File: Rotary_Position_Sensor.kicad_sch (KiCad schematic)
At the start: 8 parts

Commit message: Ещё доработать
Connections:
- net OUT_MCU: now reaches C4.2, D1.3 (OUT), R2.2
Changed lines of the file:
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@@
   (junction (at 45.72 48.26) (diameter 0) (color 0 0 0 0)
+  )
+  (junction (at 52.07 48.26) (diameter 0) (color 0 0 0 0)
   )
   (no_connect (at 55.88 38.1))
@@
     (stroke (width 0) (type default))
   )
+  (wire (pts (xy 52.07 52.07) (xy 52.07 48.26))
+    (stroke (width 0) (type default))
+  )
   (wire (pts (xy 27.94 40.64) (xy 33.02 40.64))
+    (stroke (width 0) (type default))
+  )
+  (wire (pts (xy 76.2 52.07) (xy 52.07 52.07))
     (stroke (width 0) (type default))
   )
@@
       (effects (font (size 1.27 1.27)) (justify left) hide)
     )
+  )
+  (global_label "OUT_MCU" (shape output) (at 76.2 52.07 0) (fields_autoplaced)
+    (effects (font (size 1.27 1.27)) (justify left))
+    (property "Intersheetrefs" "${INTERSHEET_REFS}" (at 87.7539 52.07 0)
+      (effects (font (size 1.27 1.27)) (justify left) hide)
+    )

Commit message: Собираю документацию
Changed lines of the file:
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@@
   (symbol (lib_id "Hall_Sensor_My:NSM3012") (at 63.5 33.02 0) (unit 1)
     (in_bom yes) (on_board yes) (dnp no) (fields_autoplaced)
-    (property "Reference" "D1" (at 63.5 29.21 0)
+    (property "Reference" "D1" (at 63.5 27.94 0)
       (effects (font (size 1.27 1.27)))
     )
-    (property "Value" "NSM3012" (at 63.5 31.75 0)
+    (property "Value" "NSM3012" (at 63.5 30.48 0)
       (effects (font (size 1.27 1.27)))
     )

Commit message: ...
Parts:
- R1: value 10 -> 0
- R2: value 50 -> 51

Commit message: Версия под отчёт
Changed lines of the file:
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@@
   )
   (symbol (lib_id "Device:C_Small") (at 174.625 99.06 0) (unit 1)
-    (in_bom yes) (on_board yes) (dnp no) (fields_autoplaced)
-    (property "Reference" "C5" (at 177.165 98.4313 0)
-      (effects (font (size 1.27 1.27)) (justify left))
-    )
-    (property "Value" "100n" (at 177.165 100.9713 0)
+    (in_bom yes) (on_board yes) (dnp no)
+    (property "Reference" "C5" (at 176.53 97.79 0)
+      (effects (font (size 1.27 1.27)) (justify left))
+    )
+    (property "Value" "100n" (at 176.53 100.33 0)
       (effects (font (size 1.27 1.27)) (justify left))
     )
@@
         )
         (path "/69677e3f-3942-4c93-9a5c-92669e2df5eb/bcde038a-9c61-4256-93bc-e646290f2e91"
-          (reference "C1") (unit 1)
+          (reference "C5") (unit 1)
         )
         (path "/69677e3f-3942-4c93-9a5c-92669e2df5eb/555e8538-1d60-4a85-8162-4c8254aec889"
@@
   (symbol (lib_id "Device:R_Small") (at 137.795 96.52 90) (unit 1)
     (in_bom yes) (on_board yes) (dnp no)
-    (property "Reference" "R1" (at 137.795 93.98 90)
-      (effects (font (size 1.27 1.27)))
-    )
-    (property "Value" "0" (at 137.795 99.06 90)
+    (property "Reference" "R1" (at 137.795 94.615 90)
+      (effects (font (size 1.27 1.27)))
+    )
+    (property "Value" "0" (at 137.795 98.425 90)
       (effects (font (size 1.27 1.27)))
     )
@@
   (symbol (lib_id "Device:C_Small") (at 131.445 107.95 0) (unit 1)
     (in_bom yes) (on_board yes) (dnp no)
-    (property "Reference" "C2" (at 126.365 106.68 0)
+    (property "Reference" "C2" (at 127.635 106.68 0)
       (effects (font (size 1.27 1.27)) (justify left))
     )
@@
         )
         (path "/69677e3f-3942-4c93-9a5c-92669e2df5eb/bcde038a-9c61-4256-93bc-e646290f2e91"
-          (reference "C4") (unit 1)
+          (reference "C2") (unit 1)
         )
         (path "/69677e3f-3942-4c93-9a5c-92669e2df5eb/555e8538-1d60-4a85-8162-4c8254aec889"
@@
   (symbol (lib_id "Device:C_Small") (at 144.145 107.95 0) (unit 1)
     (in_bom yes) (on_board yes) (dnp no)
-    (property "Reference" "C4" (at 145.415 106.68 0)
-      (effects (font (size 1.27 1.27)) (justify left))
-    )
-    (property "Value" "100n" (at 145.415 109.22 0)
+    (property "Reference" "C4" (at 146.05 106.68 0)
+      (effects (font (size 1.27 1.27)) (justify left))
+    )
+    (property "Value" "100n" (at 146.05 109.22 0)
       (effects (font (size 1.27 1.27)) (justify left))
     )
@@
         )
         (path "/69677e3f-3942-4c93-9a5c-92669e2df5eb/bcde038a-9c61-4256-93bc-e646290f2e91"
-          (reference "C5") (unit 1)
+          (reference "C4") (unit 1)
         )
         (path "/69677e3f-3942-4c93-9a5c-92669e2df5eb/555e8538-1d60-4a85-8162-4c8254aec889"
@@
   (symbol (lib_id "Device:C_Small") (at 131.445 100.33 0) (unit 1)
     (in_bom yes) (on_board yes) (dnp no)
-    (property "Reference" "C1" (at 126.365 99.06 0)
+    (property "Reference" "C1" (at 127.635 99.06 0)
       (effects (font (size 1.27 1.27)) (justify left))
     )
@@
         )
         (path "/69677e3f-3942-4c93-9a5c-92669e2df5eb/bcde038a-9c61-4256-93bc-e646290f2e91"
-          (reference "C2") (unit 1)
+          (reference "C1") (unit 1)
         )
         (path "/69677e3f-3942-4c93-9a5c-92669e2df5eb/555e8538-1d60-4a85-8162-4c8254aec889"
@@
   (symbol (lib_id "Device:C_Small") (at 144.145 100.33 0) (unit 1)
     (in_bom yes) (on_board yes) (dnp no)
-    (property "Reference" "C3" (at 145.415 99.06 0)
-      (effects (font (size 1.27 1.27)) (justify left))
-    )
-    (property "Value" "100n" (at 145.415 101.6 0)
+    (property "Reference" "C3" (at 146.05 99.06 0)
+      (effects (font (size 1.27 1.27)) (justify left))
+    )
+    (property "Value" "100n" (at 146.05 101.6 0)
       (effects (font (size 1.27 1.27)) (justify left))
     )
@@
   (symbol (lib_id "Device:R_Small") (at 137.795 111.76 90) (unit 1)
     (in_bom yes) (on_board yes) (dnp no)
-    (property "Reference" "R2" (at 137.795 109.22 90)
-      (effects (font (size 1.27 1.27)))
-    )
-    (property "Value" "51" (at 137.795 114.3 90)
-      (effects (font (size 1.27 1.27)))
-    )
+    (property "Reference" "R2" (at 137.795 109.855 90)
+      (effects (font (size 1.27 1.27)))
+    )
+    (property "Value" "51" (at 137.795 113.665 90)
+      (effects (font (size 1.27 1.27)))
+    )

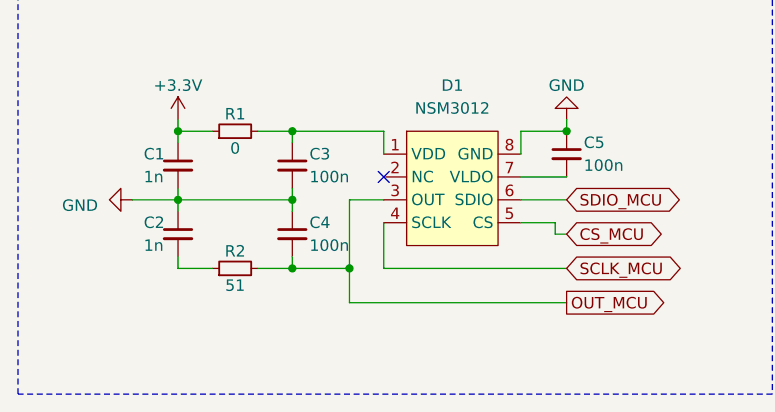
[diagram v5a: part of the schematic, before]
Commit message: Изменил разводку шунтов, вывел выход датчика положения после фильтра
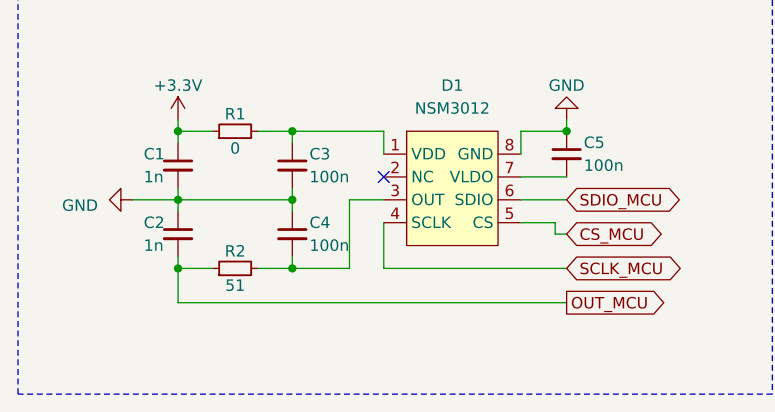
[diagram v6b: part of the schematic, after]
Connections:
- net OUT_MCU: now also C2.2, R2.1; no longer C4.2, D1.3 (OUT), R2.2
- new net: C4.2, D1.3 (OUT), R2.2
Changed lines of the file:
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@@
   (paper "A4")
   (title_block
-    (comment 1 "МПСТ.76721.758764.03.Э3.М")
+    (comment 1 "МПСТ.76721.758764.03.М Э3")
   )
   (junction (at 144.145 111.76) (diameter 0) (color 0 0 0 0)
@@
   (junction (at 131.445 104.14) (diameter 0) (color 0 0 0 0)
   )
-  (junction (at 150.495 111.76) (diameter 0) (color 0 0 0 0)
+  (junction (at 131.445 111.76) (diameter 0) (color 0 0 0 0)
   )
   (no_connect (at 154.305 101.6))
@@
     (stroke (width 0) (type default))
   )
-  (wire (pts (xy 174.625 115.57) (xy 150.495 115.57))
+  (wire (pts (xy 131.445 115.57) (xy 174.625 115.57))
     (stroke (width 0) (type default))
   )
@@
     (stroke (width 0) (type default))
   )
-  (wire (pts (xy 150.495 115.57) (xy 150.495 111.76))
-    (stroke (width 0) (type default))
-  )
   (wire (pts (xy 169.545 104.14) (xy 174.625 104.14))
     (stroke (width 0) (type default))
@@
     (stroke (width 0) (type default))
   )
+  (wire (pts (xy 131.445 115.57) (xy 131.445 111.76))
+    (stroke (width 0) (type default))
+  )

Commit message: VER2.0
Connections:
- net +3.3V renamed +3.3VA
- net CS_MCU: no longer names the net of D1.5 (CS)
- net GND renamed GNDA
- net SCLK_MCU: no longer names the net of D1.4 (SCLK)
- net SDIO_MCU: no longer names the net of D1.6 (SDIO)
- no-connect marks 1 -> 4
